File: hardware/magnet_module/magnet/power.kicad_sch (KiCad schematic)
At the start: 0 parts

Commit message: power converter design
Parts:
- added C24, C26: 1uF, symbol Device:C
- added C25: 470pF, symbol Device:C
- added C27, C28: 10uF, symbol Device:C
- added C29, C30: 0.1uF, symbol Device:C
- added C31, C32: 22uF, symbol Device:C
- added D3: UPS840E3/TR13, symbol Device:D
- added D4: 150060GS75000, symbol Device:LED
- added J20: Barrel_Jack, symbol Connector:Barrel_Jack
- added L1: 3.3uH, symbol Device:L
- added R15: 442, symbol Device:R
- added R16: 54.9k, symbol Device:R
- added R17: 10k, symbol Device:R
- added U11: MIC5219-3.3YM5, Package_TO_SOT_SMD:SOT-23-5, symbol Regulator_Linear:MIC5219-3.3YM5
- added U12: TPS565208, Package_TO_SOT_SMD:SOT-23-6, symbol Regulator_Switching:TPS565208
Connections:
- new net: C30.2, L1.1, U12.2 (SW)
- new net: C30.1, U12.6 (VBST)
- new net: C25.1, U11.4 (BP)
- new net: R16.2, R17.1, U12.4 (VFB)
- new net: D4.1 (K), R15.1
- new net: D3.2 (A), J20.1
- new net 12V: C24.1, C27.1, C28.1, C29.1, D3.1 (K), D4.2 (A), U11.1 (IN), U11.3 (EN), U12.3 (VIN), U12.5 (EN)
- new net 3V3: C26.1, U11.5 (OUT)
- new net 5V: C31.1, C32.1, L1.2, R16.1
- new net GND: C24.2, C25.2, C26.2, C27.2, C28.2, C29.2, C31.2, C32.2, J20.2, R15.2, R17.2, U11.2 (GND), U12.1 (GND)
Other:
- note added: "12V to 3V3 Converter"
- note added: "12V to 5V converter Max expected current consumption: 2.7 A"
- note added: "Aux Power In"
- note added: "Capacitor current Ico(rms) = (Vout * (Vin - Vout))/(sqrt(12) * Vin * L * f_{sw}) Ico(rms) = 1.11 A"
- note added: "Expected current consumption: 124mA Supports max 500mA"
- note added: "Inductor selection math Ipp = Vout/Vin(max) * (Vin(max) - Vout)/(Lo * fsw) Ipp = 5/12.1 * (12.1 - 5)/(3.3uH * 550 kHz) Ipp = 1.6 A Ipeak = Io + Ipp/2 = 2.7 + 0.8 = 3.5 A Io(rms) = sqrt(Io^{2} + 1/12 Ipp^{2}) = 2.74 A"
- note added: "Vf = 3.2V If = 20mA"
- note added: "Vout = 0.76*(1+R20/R21)"

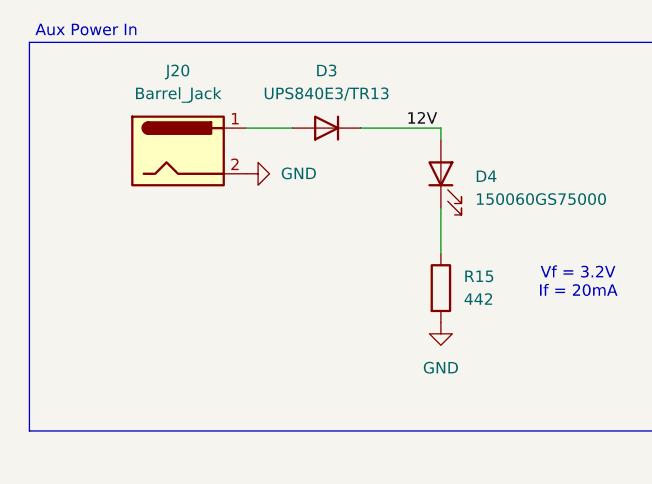
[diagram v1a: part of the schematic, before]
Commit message: fix erc errors
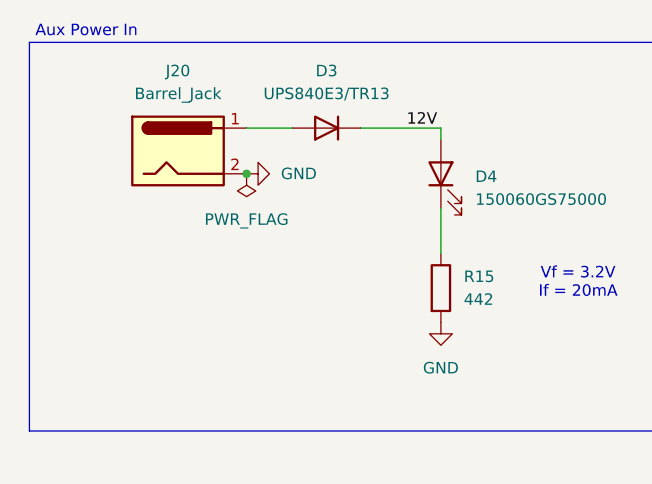
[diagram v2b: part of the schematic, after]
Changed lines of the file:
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@@
+	)
+	(junction
+		(at 39.37 33.02)
+		(diameter 0)
+		(color 0 0 0 0)
 	)
 	(junction
@@
 			)
 			(justify left)
+		)
+	)
+	(netclass_flag ""
+		(length 2.54)
+		(shape round)
+		(at 88.9 151.13 0)
+		(fields_autoplaced yes)
+		(effects
+			(font
+				(size 1.27 1.27)
+			)
+			(justify left bottom)
+		)
+		(property "Netclass" "Power"
+			(at 89.5985 148.59 0)
+			(effects
+				(font
+					(size 1.27 1.27)
+					(italic yes)
+				)
+				(justify left)
+			)
 		)
 	)
@@
 					(unit 1)
 				)
+			)
+		)
+	)
+	(symbol
+		(lib_id "power:PWR_FLAG")
+		(at 39.37 33.02 180)
+		(unit 1)
+		(exclude_from_sim no)
+		(in_bom yes)
+		(on_board yes)
+		(dnp no)
+		(fields_autoplaced yes)
+		(property "Reference" "#FLG06"
+			(at 39.37 34.925 0)
+			(effects
+				(font
+					(size 1.27 1.27)
+				)
+				(hide yes)
+			)
+		)
+		(property "Value" "PWR_FLAG"
+			(at 39.37 38.1 0)
+			(effects
+				(font
+					(size 1.27 1.27)
+				)
+			)
+		)
+		(property "Footprint" ""
+			(at 39.37 33.02 0)
+			(effects
+				(font
+					(size 1.27 1.27)
+				)
+				(hide yes)
+			)
+		)
+		(property "Datasheet" "~"
+			(at 39.37 33.02 0)
+			(effects
+				(font
+					(size 1.27 1.27)
+				)
+				(hide yes)
+			)
+		)
+		(property "Description" "Special symbol for telling ERC where power comes from"
+			(at 39.37 33.02 0)
+			(effects
+				(font
+					(size 1.27 1.27)
+				)
+				(hide yes)
+			)
+		)
+		(pin "1"
+		)
+		(instances
+			(project "magnet"
+				(path "/aa5044b8-67cd-4b5a-a593-0df9431eb095/2d556af5-2e8e-4584-962b-364bdedf6f87"
+					(reference "#FLG06")
+					(unit 1)
+				)
